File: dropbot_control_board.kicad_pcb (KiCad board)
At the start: 2 copper layers, 83.6 x 69.2 mm, 91 parts, among them IC1 MCP6024, J2 COMM_BUS, P1 FEEDBACK, P3 POWER, P4 VOUT, P5 LIGHT, P6 MAGNET, P7 CONN_01X04, P8 CONN_01X03, Q1 IRF644PBF, Q2 TIP120, Q3 2N7002, Q4 2N7002, Q5 Q_NMOS_GDS, Q6 Q_NMOS_GDS, U1 Teensy_3.2, U2 MAX1771, U3 MCP41050, U4 HV7802, U5 AQW216, U6 NCP5304, U7 AQW216, U8 AQW216

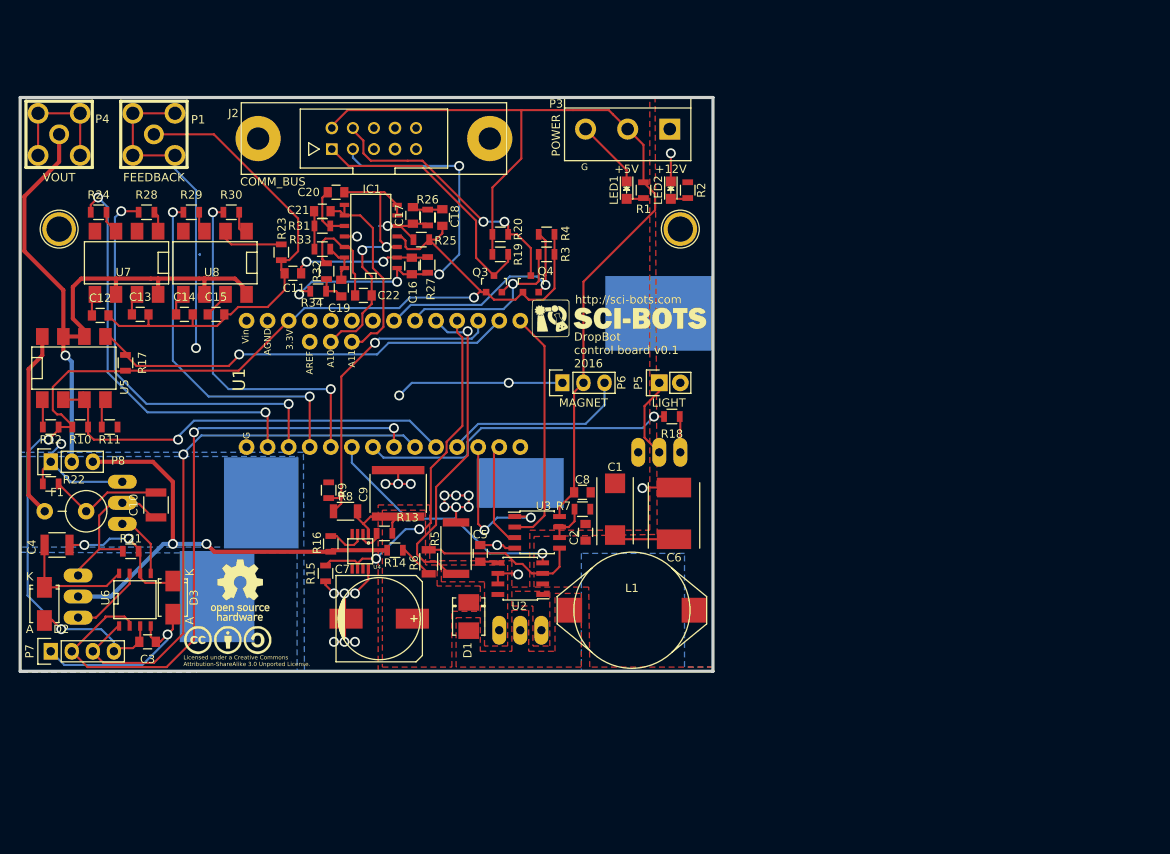
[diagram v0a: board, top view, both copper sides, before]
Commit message: Minor fixes
* fix inductor footprint
* footprints for various HV resistors
* labels for some resistors/caps
* remove shorted +12V trace
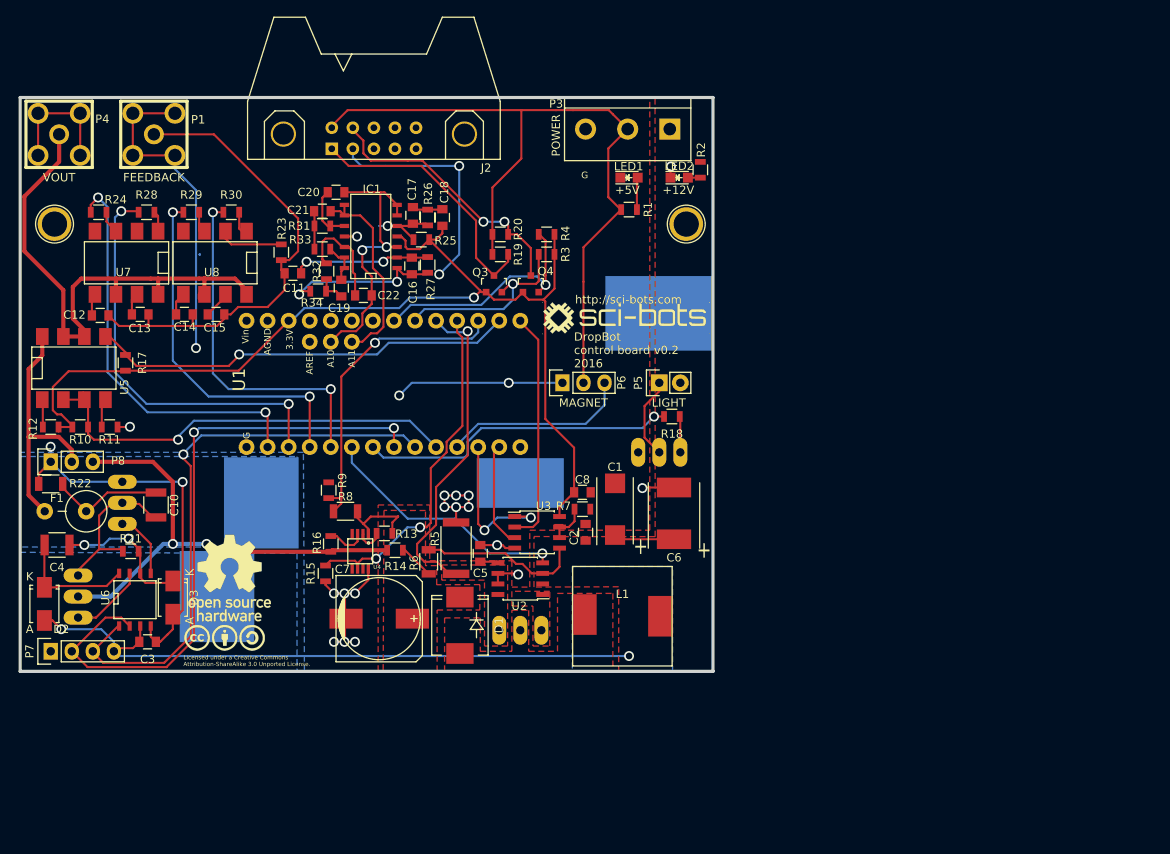
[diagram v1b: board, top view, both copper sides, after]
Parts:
- removed C9: 100nF,400V, Capacitors_SMD:C_2225
- removed the G*** at (49.4, 89.2)
- removed the G*** at (50.9, 83.2)
- removed the G*** at (96.6, 50.4)
- added G***: LOGO, LOGO, F.Cu at (97.5, 50.3)
- added G***: LOGO, footprints:OSHW_logo_10mm, F.Cu at (49.7, 81.7)
- added G***: LOGO, footprints:CC_S_A_logo_10mm, F.Cu at (49.0, 88.9)
- C10: value C -> 100n,500V
- C19: value 4.7nF -> 0.015uF
- C20, C22: value 1nF -> 100pF
- C21: value 0.15uF -> 470pF
- C4: value 0.1uF -> 100n,500V
- D1: value ES2F -> ES3J; footprint Diodes_SMD:DO-214BA -> Diodes_SMD:SMC_Standard
- J2: footprint Connect:he10-10d -> Connect:HE10-10C
- L1: value 100uH -> 47uH,3.8A; footprint footprints:DU1971 -> footprints:SRR1210
- Q1: value IRF644PBF -> STP33N65M2
- Q5, Q6: value Q_NMOS_GDS -> IRF740BPBF
- R22: value R -> 2M; footprint Resistors_SMD:R_0805 -> Resistors_SMD:R_1206
- R31: value 1.91k -> 18.7k
- R32: value 16.9k -> 2.1k
- R33: value 806 -> 14.7k
- R34: value 13.3k -> 887
- R5: value 50m -> 30m
- R6, R8: value 1M -> 2M
- R7: value 4k -> 2k
- U5, U7, U8: value AQW216 -> DPST (2 Form A), 350V
- moved R1 2.92 mm to (97.8, 37.3), turned to 0 degrees
- moved R2 2.89 mm to (106.4, 32.5)
- moved LED2 1.81 mm to (103.9, 33.4), turned to 0 degrees
- moved LED1 1.53 mm to (97.8, 33.4), turned to 0 degrees
- moved D1 1.50 mm to (77.4, 87.4)
- moved L1 1.35 mm to (97.0, 86.3)
- moved REF** 0.94 mm to (104.7, 39.0)
- moved REF** 0.82 mm to (28.5, 39.0)
- turned J2 to 180 degrees
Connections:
- C3 pad 2: +3.3V -> +12V
- C8 pad 2: +5V -> +3.3V
- D2 pad 2: +3.3V -> +12V
- P7 pad 4: +3.3V -> +12V
- P8 pad 2: VOUT -> HVAC
- U3 pad 8: +5V -> +3.3V
- U6 pad 3: +3.3V -> +12V
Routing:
- net +12V: track 7.32 -> 85.5 mm, vias 0 -> 2
- net +5V: track 109.4 -> 90.7 mm
- net VOUT: track 81.7 -> 66.1 mm, vias 1 -> 0
- net +3.3V: track 143.3 -> 128.3 mm, vias 3 -> 1
- net HVAC: track 22.6 -> 29.9 mm
- net GND: track 210.8 -> 204.9 mm, vias 27 -> 25
- net Net-(LED1-Pad2): track 2.07 -> 4.34 mm
- net D7/DRIVER_LO: track 68.6 -> 70.1 mm
- net Net-(C10-Pad2): track 14.8 -> 13.9 mm
- net D13/SCK: track 28.9 -> 28.2 mm
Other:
- board text added: "+"
- board text added: "DropBot control board v0.2 2016"
- board text removed: "DropBot control board v0.1 2016"

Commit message: Use edge connectors and ...
* Add SPI flash memory
* Add HV output enable
* Make feedback circuit breakout and use DIP op-amp
* Pass Teensy's USB signals through edge connector
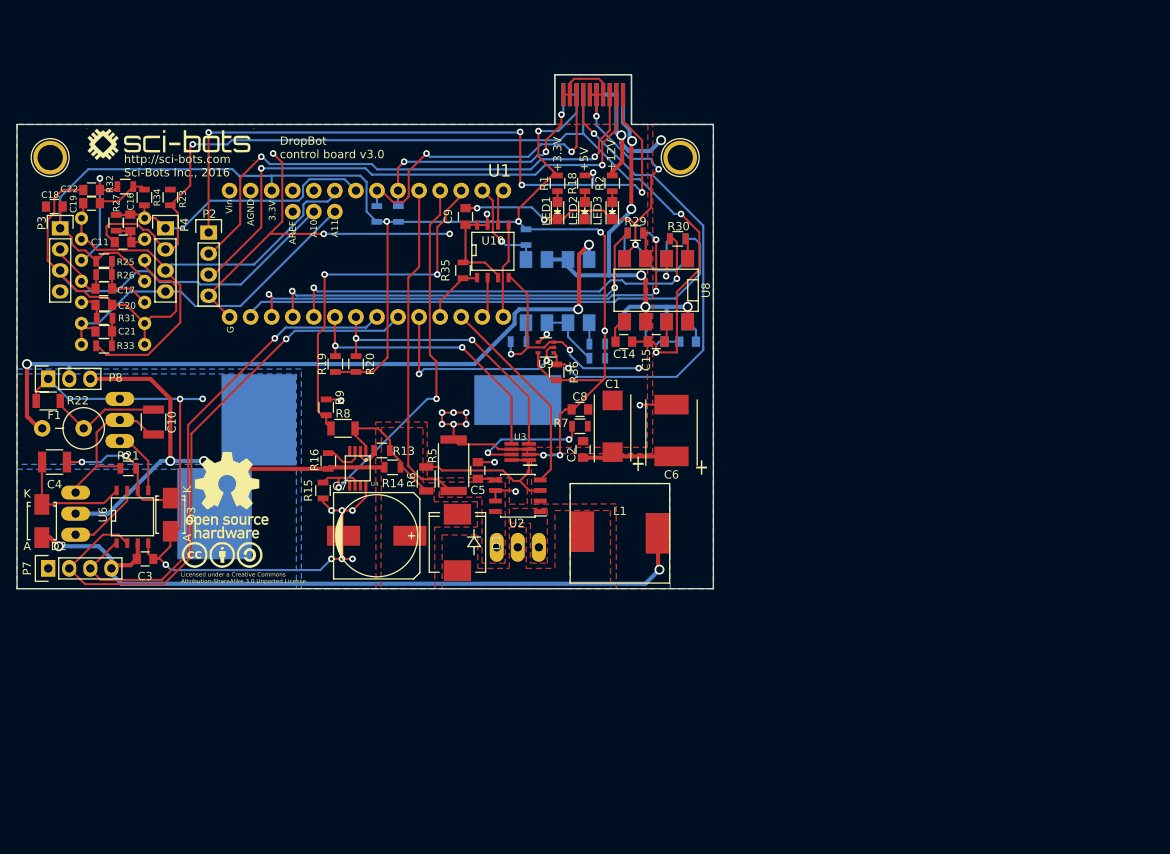
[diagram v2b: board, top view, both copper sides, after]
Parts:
- removed J2: COMM_BUS, Connect:HE10-10C
- removed P5: LIGHT, Pin_Headers:Pin_Header_Straight_1x02
- removed P6: MAGNET, Pin_Headers:Pin_Header_Straight_1x03
- removed Q2: TIP120, TO_SOT_Packages_THT:TO-220_Neutral123_Horizontal_LargePads
- removed Q3, Q4: 2N7002, TO_SOT_Packages_SMD:SOT-23
- added C9: 0.1uF, Capacitors_SMD:C_0805, F.Cu at (78.1, 38.1)
- added LED3: +12V, LEDs:LED_0805, F.Cu at (95.8, 37.4)
- added P2: CONN_01X04, Pin_Headers:Pin_Header_Straight_1x04, F.Cu at (47.1, 40.0)
- added R35: 5.1k, Resistors_SMD:R_0805, F.Cu at (77.8, 44.6)
- added R36: 4.75k, Resistors_SMD:R_0805, F.Cu at (89.1, 56.9)
- added U10: W25Q64FV, SMD_Packages:SOIC-8-N, F.Cu at (81.4, 42.3)
- added U9: 74AHC1G32, TO_SOT_Packages_SMD:SOT-353, F.Cu at (87.8, 53.9)
- C12, C13, R10, R11, R12, R17, R24, R28, R3, R4, U5, U7: moved to B.Cu
- IC1: footprint SMD_Packages:SOIC-14_N -> Housings_DIP:DIP-14_W7.62mm; moved to B.Cu
- LED1: value +5V -> +3.3V
- LED2: value +12V -> +5V
- P1: value FEEDBACK -> CONN_02X10; footprint footprints:JACK_SMA -> WheelerLab:HSEC8-110-XX-X-RA-MATE
- P3: value POWER -> CONN_01X04; footprint Connect:bornier3 -> Pin_Headers:Pin_Header_Straight_1x04
- P4: value VOUT -> CONN_01X04; footprint footprints:JACK_SMA -> Pin_Headers:Pin_Header_Straight_1x04
- U3: value MCP41050 -> CAT5171; footprint Housings_SOIC:SOIC-8_3.9x4.9mm_Pitch1.27mm -> WheelerLab:SOT-23-8
- moved C12 70.9 mm to (104.9, 53.2), turned to 180 degrees
- moved R24 69.9 mm to (103.7, 40.8), turned to 180 degrees
- moved P3 69.5 mm to (29.2, 39.5), turned to 0 degrees
- moved R12 66.7 mm to (94.0, 53.5)
- moved U7 64.0 mm to (101.1, 47.0), turned to 0 degrees
- moved R10 62.9 mm to (94.0, 55.2), turned to 180 degrees
- moved C13 62.3 mm to (101.1, 53.2)
- moved U5 59.1 mm to (89.2, 47.1), turned to 180 degrees
- moved R28 59.0 mm to (98.6, 40.1), turned to 180 degrees
- moved G*** 58.8 mm to (42.5, 29.4)
- moved R30 53.9 mm to (103.7, 40.8)
- moved R29 53.6 mm to (98.6, 40.1)
- moved U8 53.3 mm to (101.1, 47.0)
- moved C15 53.2 mm to (101.1, 53.2), turned to 180 degrees
- moved C14 53.1 mm to (97.2, 53.2)
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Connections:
- C16 pad 1: Net-(C16-Pad1) -> A6
- C19 pad 1: Net-(C19-Pad1) -> A7
- IC1 pad 1: Net-(C16-Pad1) -> A6
- IC1 pad 13: Net-(C19-Pad1) -> A7
- IC1 pad 14: Net-(C19-Pad1) -> A7
- LED2 pad 1: GND -> Net-(LED2-Pad1)
- P1 pad 1: CUR_SENSE -> SDA
- P3 pad 1: +12V -> +3.3V
- P3 pad 2: +5V -> GND
- P3 pad 3: GND -> +0.6V
- P4 pad 1: VOUT -> A6
- P4 pad 2: GND -> CUR_SENSE
- P7 pad 2: D6/DRIVER_HI -> D7/DRIVER_HI
- P7 pad 3: D7/DRIVER_LO -> D6/DRIVER_LO
- R1 pad 1: +5V -> +3.3V
- R10 pad 2: D8/OUTPUT_SELECT -> Net-(R10-Pad2)
- R18 pad 1: Net-(Q2-Pad1) -> +5V
- R18 pad 2: D5/LED -> Net-(LED2-Pad2)
- R19 pad 1: +5V -> D4/SSDA
- R19 pad 2: SDA_5V -> +3.3V
- R2 pad 2: Net-(LED2-Pad2) -> Net-(LED3-Pad2)
- R20 pad 1: +5V -> D5/SSCL
- R20 pad 2: SCL_5V -> +3.3V
- R27 pad 1: Net-(C16-Pad1) -> A6
- R3 pad 2: SDA_3.3V -> SDA
- R33 pad 1: Net-(C19-Pad1) -> A7
- R34 pad 1: Net-(C16-Pad1) -> A6
- R4 pad 2: SCL_3.3V -> SCL
- U1 pad 10: D10/MCP41050_CS -> D10/SHDN
- U1 pad 11: D11/MOSI -> D11/DI
- U1 pad 12: D12/MISO -> D12/DO
- U1 pad 13: D13/SCK -> D13/CLK
- U1 pad 18: SDA_3.3V -> SDA
- U1 pad 19: SCL_3.3V -> SCL
- U1 pad 20: Net-(U1-Pad20) -> A6
- U1 pad 21: Net-(U1-Pad21) -> A7
- U1 pad 4: D4/SHDN -> D4/SSDA
- U1 pad 5: D5/LED -> D5/SSCL
- U1 pad 6: D6/DRIVER_HI -> D6/DRIVER_LO
- U1 pad 7: D7/DRIVER_LO -> D7/DRIVER_HI
- U1 pad 9: D9/SERVO -> D9/CS
- U2 pad 4: D4/SHDN -> D10/SHDN
- U3 pad 1: D10/MCP41050_CS -> Net-(R6-Pad2)
- U3 pad 2: D13/SCK -> +3.3V
- U3 pad 3: D11/MOSI -> GND
- U3 pad 4: GND -> D5/SSCL
- U3 pad 5: Net-(R6-Pad2) -> D4/SSDA
- U3 pad 6: Net-(R7-Pad1) -> GND
- U3 pad 8: +3.3V -> Net-(R6-Pad2)
- U5 pad 2: D8/OUTPUT_SELECT -> Net-(R10-Pad2)
- U5 pad 3: D8/OUTPUT_SELECT -> Net-(R10-Pad2)
- U6 pad 1: D7/DRIVER_LO -> D6/DRIVER_LO
- U6 pad 2: D6/DRIVER_HI -> D7/DRIVER_HI
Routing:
- net D6/DRIVER_HI: track 77.7 -> 0.00 mm, vias 2 -> 0
- net +3.3V: track 128.3 -> 203.8 mm, vias 1 -> 8
- net GND: track 204.9 -> 278.0 mm, vias 25 -> 31
- net D7/DRIVER_HI: track 0.00 -> 71.6 mm, vias 0 -> 1
- net D7/DRIVER_LO: track 70.1 -> 0.00 mm, vias 1 -> 0
- net D+: track 0.00 -> 67.0 mm, vias 0 -> 2
- net CUR_SENSE: track 58.7 -> 124.5 mm, vias 0 -> 3
- net D-: track 0.00 -> 64.2 mm, vias 0 -> 2
- net D6/DRIVER_LO: track 0.00 -> 61.9 mm, vias 0 -> 1
- net A7: track 0.00 -> 61.2 mm
- net HV_OE: track 0.00 -> 61.0 mm, vias 0 -> 2
- net HVAC: track 29.9 -> 90.6 mm, vias 0 -> 3
- net +0.6V: track 34.3 -> 80.2 mm, vias 2 -> 0
- net A0/SHORT_CHK: track 51.6 -> 12.0 mm
- net D5/LED: track 38.6 -> 0.00 mm, vias 1 -> 0
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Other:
- board size 83.6 x 69.2 mm -> 84 x 62 mm
- net class Default: via_dia 1.2 -> 0.8; via_drill 0.8 -> 0.4
- board text added: "DropBot control board v3.0"
- board text added: "http://sci-bots.com Sci-Bots Inc., 2016"
- board text removed: "DropBot control board v0.2 2016"
- board text removed: "G"
- board text removed: "http://sci-bots.com"

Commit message: EMC related improvements
* convert to 4-layer board
* add jumper to connect 3.3V of Teensy
* put filters on i2c
* add guard traces around i2c and current-sense lines
* add ferrites to SPI lines
* add snubber on SPMS diode
* add pads for gate driver current limiting resistors
* add LPF to HV driver
* add PTC fuse and voltage clamp to feedback (current-sense) signal
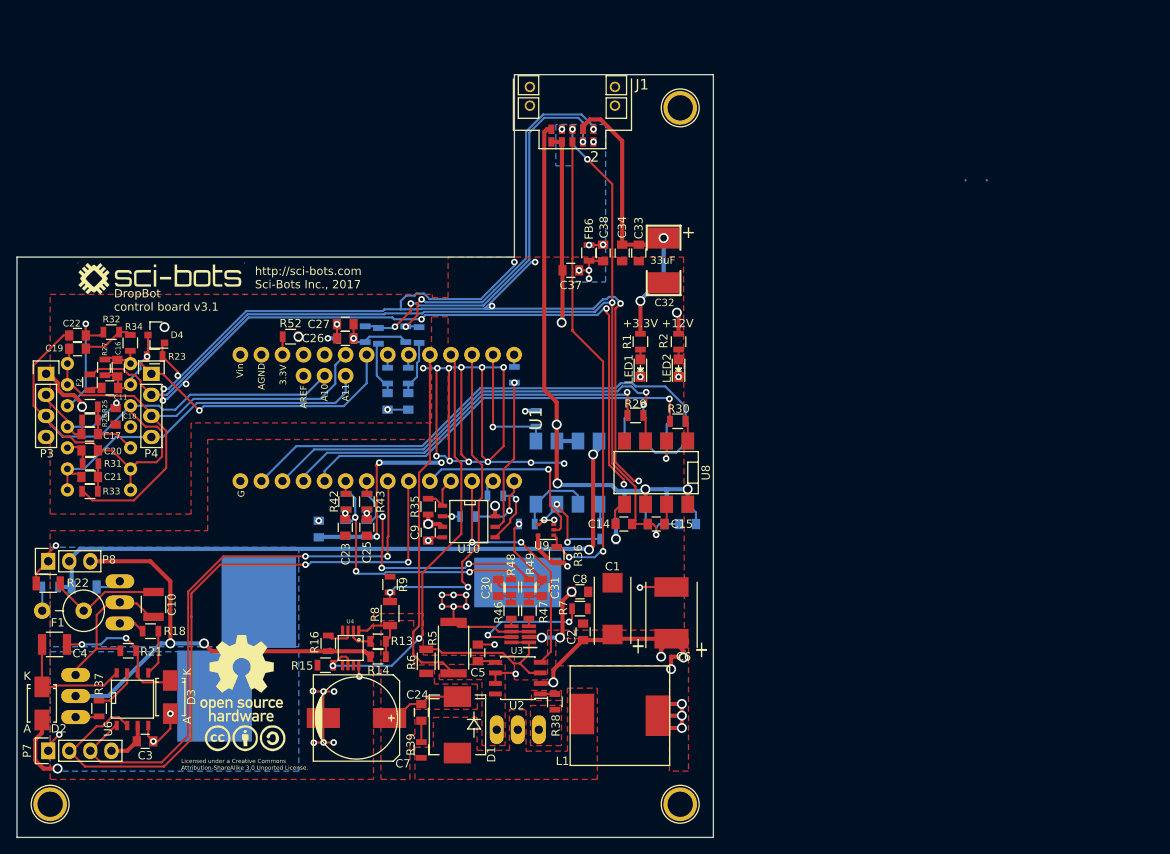
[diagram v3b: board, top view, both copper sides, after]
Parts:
- removed the LED2 at (92.5, 37.4)
- removed REF** (x2): 1pin, Connect:1pin
- added C23: C_Small, Capacitors_SMD:C_0805, F.Cu at (63.6, 75.6)
- added C24: 1000pF, Capacitors_SMD:C_0805, F.Cu at (72.8, 97.9)
- added C25: C_Small, Capacitors_SMD:C_0805, F.Cu at (66.2, 75.6)
- added C26: 0.1uF, Capacitors_SMD:C_0805, F.Cu at (63.6, 52.8)
- added C27: 0.01uF, Capacitors_SMD:C_0805, F.Cu at (63.6, 51.1)
- added C28: C, Capacitors_SMD:C_0805, B.Cu at (68.7, 60.4)
- added C29: C, Capacitors_SMD:C_0805, B.Cu at (71.2, 60.4)
- added C30: C_Small, Capacitors_SMD:C_0805, F.Cu at (82.0, 82.9)
- added C31: C_Small, Capacitors_SMD:C_0805, F.Cu at (87.3, 82.9)
- added C32: 33uF, WheelerLab:SM2917, F.Cu at (102.0, 43.4)
- added C33: 0.1uF, Capacitors_SMD:C_0805, F.Cu at (99.0, 42.5)
- added C34: 0.01uF, Capacitors_SMD:C_0805, F.Cu at (97.0, 42.5)
- added C35: C, Capacitors_SMD:C_1206, B.Cu at (32.1, 82.8)
- added C36: 0.1uF, Capacitors_SMD:C_0805, B.Cu at (60.4, 75.8)
- added C37: 0.1uF, Capacitors_SMD:C_0805, F.Cu at (90.8, 44.6)
- added C38: 0.1uF, Capacitors_SMD:C_0805, F.Cu at (94.7, 42.5)
- added D4: BAV99, TO_SOT_Packages_SMD:SOT-23, F.Cu at (40.8, 52.4)
- added F2: PTC 30mA, Resistors_SMD:R_0805, F.Cu at (32.8, 58.1)
- added FB1: FERRITE, Resistors_SMD:R_0805, B.Cu at (63.7, 52.8)
- added FB2: FERRITE, Resistors_SMD:R_0805, B.Cu at (28.0, 82.8)
- added FB3: FERRITE, Resistors_SMD:R_0805, B.Cu at (78.4, 74.3)
- added FB4: FERRITE, Resistors_SMD:R_0805, B.Cu at (81.7, 71.8)
- added FB5: FERRITE, Resistors_SMD:R_0805, B.Cu at (84.0, 57.2)
- added FB6: FERRITE, Resistors_SMD:R_0805, F.Cu at (93.0, 42.5)
- added J1: TFM-105-02-X-DH, WheelerLab:TFM-105-02-X-DH, F.Cu at (91.0, 21.0)
- added P5: CONN_01X01, Connect:1pin, F.Cu at (28.0, 109.0)
- added R37: 10, Resistors_SMD:R_0805, F.Cu at (33.9, 97.5)
- added R38: 10, Resistors_SMD:R_0805, F.Cu at (88.9, 96.7)
- added R39: 10, Resistors_SMD:R_0805, F.Cu at (72.8, 102.5)
- added R40: R, Resistors_SMD:R_0805, B.Cu at (63.7, 72.5)
- added R41: R, Resistors_SMD:R_0805, B.Cu at (66.2, 72.5)
- added R42: R, Resistors_SMD:R_0805, F.Cu at (63.7, 72.5)
- added R43: R, Resistors_SMD:R_0805, F.Cu at (66.2, 72.5)
- added R44: R, Resistors_SMD:R_0805, B.Cu at (68.7, 57.3)
- added R45: R, Resistors_SMD:R_0805, B.Cu at (71.2, 57.3)
- added R46: R, Resistors_SMD:R_0805, F.Cu at (83.6, 85.7)
- added R47: R, Resistors_SMD:R_0805, F.Cu at (85.8, 85.7)
- added R48: R, Resistors_SMD:R_0805, F.Cu at (83.6, 82.8)
- added R49: R, Resistors_SMD:R_0805, F.Cu at (85.8, 82.8)
- added R50: R, Resistors_SMD:R_0805, B.Cu at (67.6, 52.5)
- added R51: R, Resistors_SMD:R_0805, B.Cu at (72.5, 52.4)
- added R52: 0R, Resistors_SMD:R_0805, F.Cu at (57.0, 52.6)
- F1: value FUSE -> PTC
- P1: value CONN_02X10 -> CONN_01X01; footprint WheelerLab:HSEC8-110-XX-X-RA-MATE -> Connect:1pin
- P2: value CONN_01X04 -> CONN_01X01; footprint Pin_Headers:Pin_Header_Straight_1x04 -> Connect:1pin
- R18: value 1k -> 10
- R19, R20: value 5.1k -> 4.75k; moved to B.Cu
- R3, R35, R4: value 5.1k -> 4.75k
- moved P2 89.4 mm to (104.0, 109.0)
- moved R18 75.3 mm to (40.1, 88.1), turned to 0 degrees
- moved C9 38.4 mm to (73.6, 76.2), turned to 270 degrees
- moved U10 32.7 mm to (78.5, 74.9), turned to 270 degrees
- moved R35 28.8 mm to (73.6, 73.1), turned to 270 degrees
- moved C18 26.4 mm to (35.9, 62.2), turned to 90 degrees
- moved R8 23.0 mm to (69.0, 86.0), turned to 270 degrees
- moved R13 23.0 mm to (67.5, 89.3)
- moved R14 22.9 mm to (67.5, 91.2)
- moved R9 22.7 mm to (69.0, 82.5)
- moved G*** 22.3 mm to (51.5, 101.0)
- moved G*** 22.2 mm to (51.1, 93.8)
- moved C7 22.1 mm to (65.0, 98.6)
- moved R11 22.0 mm to (85.5, 75.2)
- moved C1 22.0 mm to (95.8, 85.4)
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- renumbered LED3 to LED2
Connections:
- C11 pad 2: CUR_SENSE -> Net-(C11-Pad2)
- C18 pad 1: +3.3V -> Net-(C18-Pad1)
- F1 pad 2: HVAC -> Net-(F1-Pad2)
- P1 pad 1: SDA -> CHASIS_GND
- P2 pad 1: +5V -> CHASIS_GND
- R12 pad 1: Net-(R12-Pad1) -> +3.3V
- R12 pad 2: +3.3V -> Net-(R12-Pad2)
- R18 pad 1: +5V -> Net-(Q6-Pad1)
- R18 pad 2: Net-(LED2-Pad2) (its old number) -> Net-(R18-Pad2)
- R19 pad 1: D4/SSDA -> D5/SSCL
- R20 pad 1: D5/SSCL -> D4/SSDA
- R23 pad 1: CUR_SENSE -> Net-(C11-Pad1)
- R3 pad 1: +3.3V -> Net-(C26-Pad2)
- R4 pad 1: +3.3V -> Net-(C26-Pad2)
- U1 pad 11: D11/DI -> Net-(FB4-Pad2)
- U1 pad 12: D12/DO -> D12/MISO
- U1 pad 13: D13/CLK -> Net-(FB5-Pad1)
- U1 pad 18: SDA -> Net-(R45-Pad2)
- U1 pad 19: SCL -> Net-(R44-Pad2)
- U1 pad 24: +3.3V -> Net-(R52-Pad2)
- U1 pad 4: D4/SSDA -> Net-(R42-Pad1)
- U1 pad 5: D5/SSCL -> Net-(R43-Pad1)
- U10 pad 2: D11/DI -> Net-(FB3-Pad2)
- U10 pad 5: D12/DO -> D11/M0SI
- U2 pad 1: Net-(Q1-Pad1) -> Net-(R38-Pad2)
- U3 pad 4: D5/SSCL -> Net-(R47-Pad2)
- U3 pad 5: D4/SSDA -> Net-(R46-Pad2)
- U5 pad 1: Net-(R12-Pad1) -> Net-(R12-Pad2)
- U5 pad 2: Net-(R10-Pad2) -> Net-(R11-Pad2)
- U6 pad 5: Net-(Q6-Pad1) -> Net-(R18-Pad2)
- U6 pad 7: Net-(Q5-Pad1) -> Net-(R37-Pad2)
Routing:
- net +3.3V: track 203.8 -> 99.8 mm, vias 8 -> 17
- net +5V: track 86.6 -> 0.00 mm, vias 5 -> 0
- net (no net): track 0.14 -> 83.3 mm, vias 0 -> 12
- net D+: track 67.0 -> 0.00 mm, vias 2 -> 0
- net D-: track 64.2 -> 0.00 mm, vias 2 -> 0
- net +12V: track 119.2 -> 82.3 mm, vias 4 -> 10
- net GND: track 278.0 -> 313.9 mm, vias 31 -> 47
- net VOUT: track 56.4 -> 73.9 mm, vias 5 -> 4
- net SDA: track 31.0 -> 45.9 mm
- net D13/CLK: track 4.41 -> 18.6 mm, vias 0 -> 1
- net D12/DO: track 11.4 -> 0.00 mm
- net SCL: track 38.5 -> 48.9 mm, vias 2 -> 3
- net D7/DRIVER_HI: track 71.6 -> 81.3 mm, vias 1 -> 2
- net Net-(C26-Pad2): track 0.00 -> 8.86 mm, vias 0 -> 1
- net D6/DRIVER_LO: track 61.9 -> 70.5 mm, vias 1 -> 2
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- added copper zone on POWER, net +12V
- added copper zone on POWER, net +3.3V
- added copper zone on GND, net CHASIS_GND
- added copper zone on GND, net GND
- added copper zone on F.Cu, net Net-(R38-Pad2)
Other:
- board size 84 x 62 mm -> 84 x 92 mm
- copper layers 2 -> 4
- board text added: "DropBot control board v3.1"
- board text added: "http://sci-bots.com Sci-Bots Inc., 2017"
- board text removed: "DropBot control board v3.0"
- board text removed: "http://sci-bots.com Sci-Bots Inc., 2016"
